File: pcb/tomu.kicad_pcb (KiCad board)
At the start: 2 copper layers, 13 x 9.4 mm, 17 parts, among them P3 USB-PCB, U1 EFM32HG309

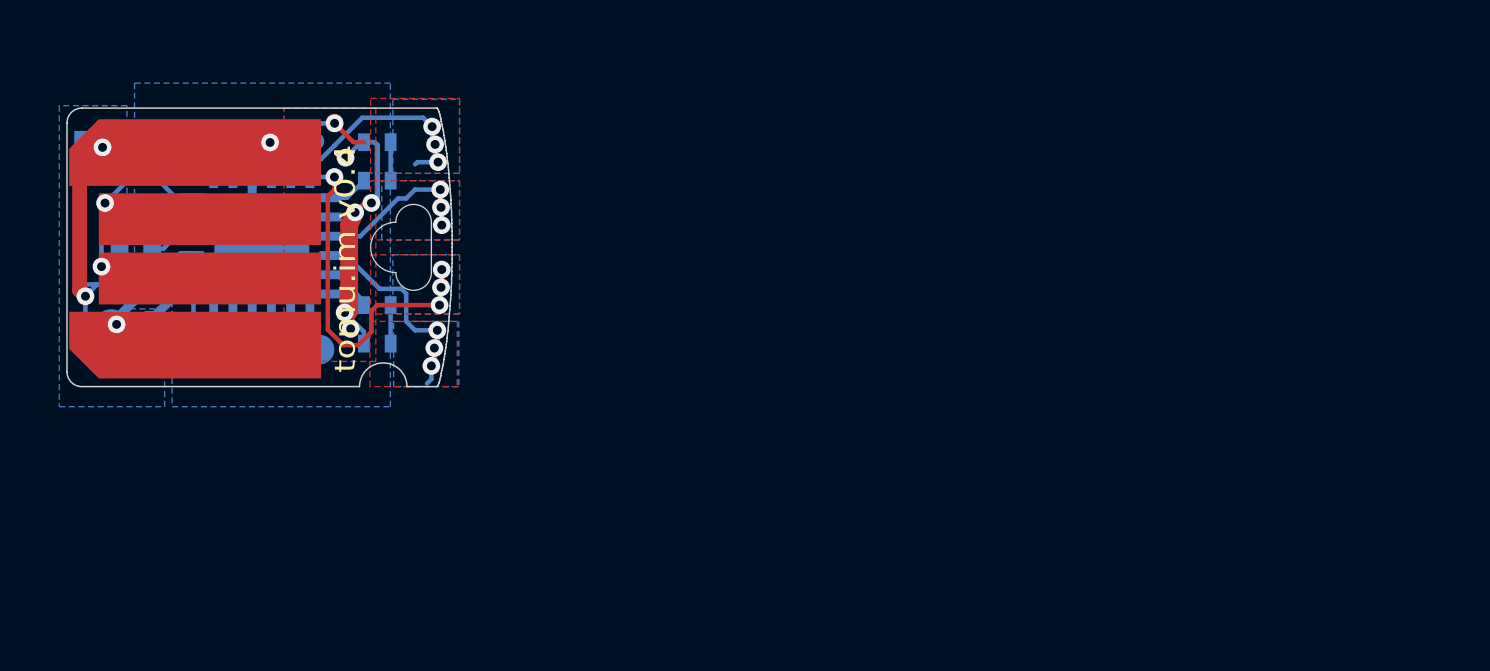
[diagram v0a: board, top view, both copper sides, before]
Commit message: Add 2.54 pinhead version for easy developing
Signed-off-by: Zamir SUN <sztsian@gmail.com>
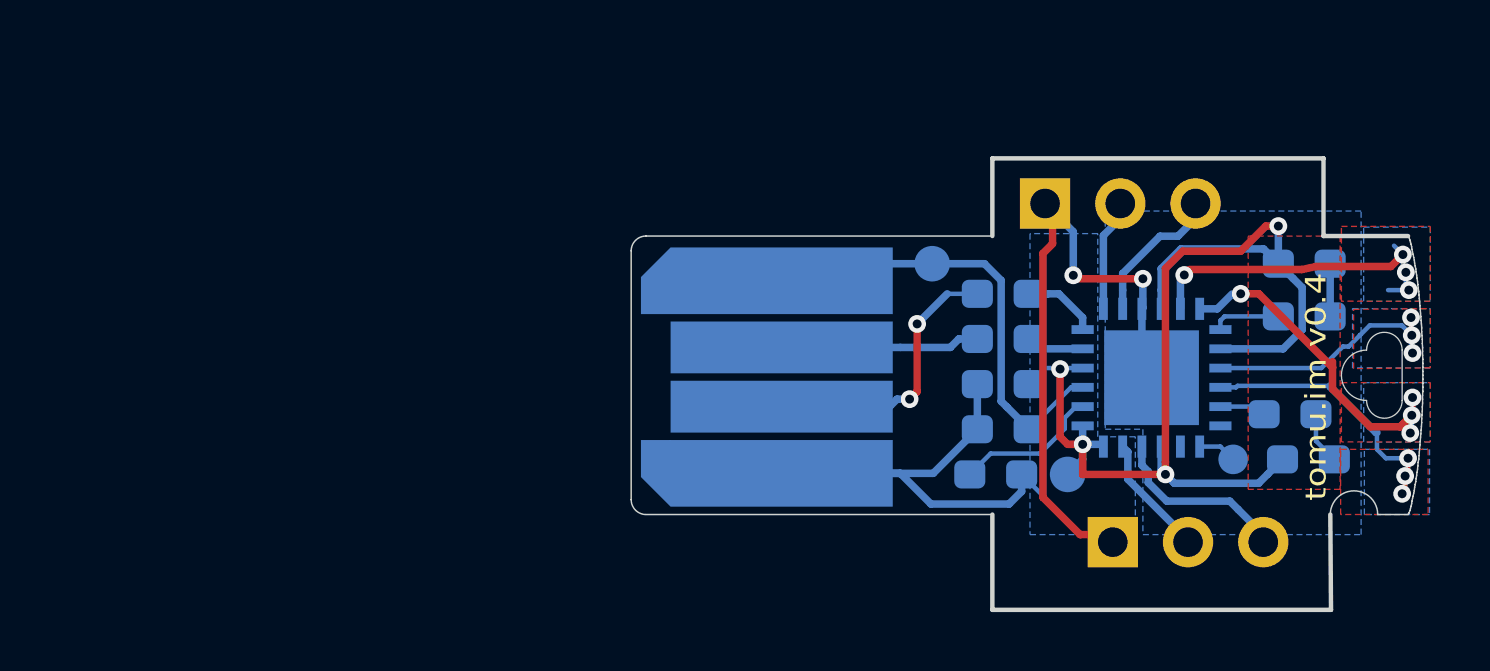
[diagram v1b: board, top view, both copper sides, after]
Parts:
- removed 3.3V: 3V_PAD, usb-pcb:pads-1x1
- removed Reset: RESET_PAD, usb-pcb:pads-1x1
- removed SWD headers: DEBUG, pads-1x3
- removed Serial headers: USART0, pads-1x3-slim
- removed USB power: 5V_PAD, usb-pcb:pads-1x1
- added P1: USART0, Connector_PinHeader_2.54mm:PinHeader_1x03_P2.54mm_Vertical, B.Cu at (52.3, 31.8)
- added P2: DEBUG, Connector_PinHeader_2.54mm:PinHeader_1x03_P2.54mm_Vertical, B.Cu at (50.0, 20.3)
- added P4: RESET_PAD, usb-pcb:pads-1x1, B.Cu at (56.4, 26.6)
- added P5: 5V_PAD, usb-pcb:pads-1x1, B.Cu at (48.6, 22.4)
- added P6: 3V_PAD, usb-pcb:pads-1x1, B.Cu at (50.8, 29.5)
- C1, C2, C3: footprint Capacitors_SMD:C_0402 -> Capacitor_SMD:C_0603_1608Metric_Pad1.05x0.95mm_HandSolder
- D1, D2: footprint LEDs:LED_0402 -> LED_SMD:LED_0603_1608Metric_Pad1.05x0.95mm_HandSolder
- P3: footprint USB-PCB -> usb-pcb:USB-PCB; moved to B.Cu
- R1, R2, R3, R4: footprint Resistors_SMD:R_0402 -> Resistor_SMD:R_0603_1608Metric_Pad1.05x0.95mm_HandSolder
- moved XX1 33.0 mm to (62.0, 26.2)
- moved D2 31.7 mm to (58.9, 29.0)
- moved R1 31.6 mm to (58.8, 24.1)
- moved D1 31.6 mm to (58.8, 22.4)
- moved R2 31.0 mm to (58.3, 27.4)
- moved U1 30.4 mm to (53.6, 26.2)
- moved C3 29.7 mm to (48.6, 27.9)
- moved C2 29.6 mm to (48.6, 26.4)
- moved R3 29.4 mm to (48.6, 24.9)
- moved R4 29.4 mm to (48.6, 23.4)
- moved C1 28.9 mm to (48.4, 29.5), turned to 180 degrees
- moved P3 20.4 mm to (36.1, 20.7)
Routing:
- net GND: track 25.5 -> 49.9 mm, vias 3 -> 2
- net +3V3: track 20.7 -> 41.7 mm, vias 6 -> 4
- net /USB_5V: track 9.02 -> 15.7 mm, vias 1 -> 0
- net /LEU0_TX: track 1.44 -> 6.14 mm
- net /USB_D+: track 5.36 -> 9.52 mm, vias 1 -> 2
- net /CAP0A: track 5.59 -> 9.66 mm
- net /USB_D-: track 2.97 -> 6.72 mm, vias 1 -> 0
- net /DBG_SWDIO: track 1.21 -> 4.82 mm
- net /CAP0B: track 8.45 -> 11.6 mm, vias 3 -> 4
- net /LEU0_RX: track 1.60 -> 3.98 mm
- net /CAP1A: track 8.64 -> 10.5 mm
- net /DEC: track 3.43 -> 4.97 mm
- net Net-(D1-Pad1): track 1.30 -> 2.79 mm
- net /CAP1B: track 12.4 -> 10.9 mm
- net /DBG_SWCLK: track 2.32 -> 3.64 mm
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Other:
- board size 13 x 9.4 mm -> 26.7 x 15.2 mm
- board text added: "RST"
- board text added: "T R G"
- board text removed: "3V"
- board text removed: "R"
- board text removed: "T"
- board text removed: "X"
